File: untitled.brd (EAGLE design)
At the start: 59.4 x 57.8 mm, 25 parts

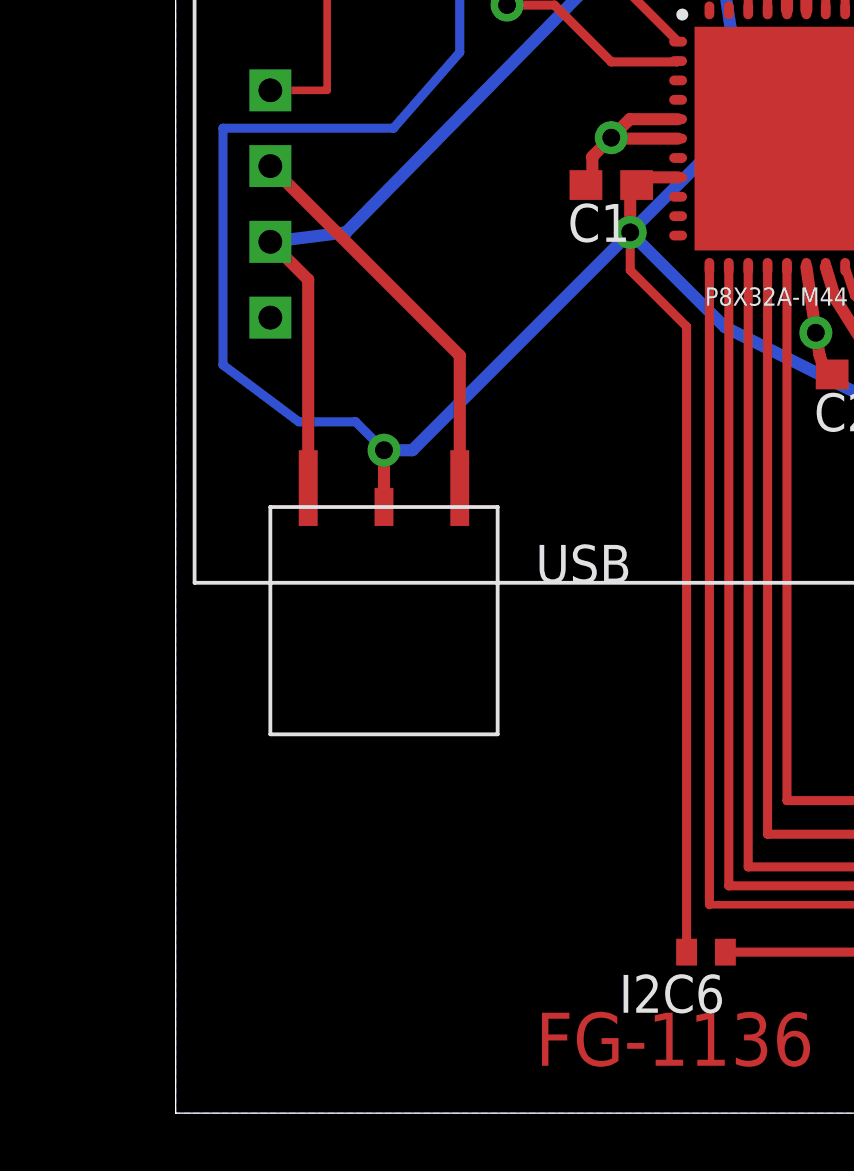
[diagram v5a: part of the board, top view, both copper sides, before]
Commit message: Use regulator part from eagle library
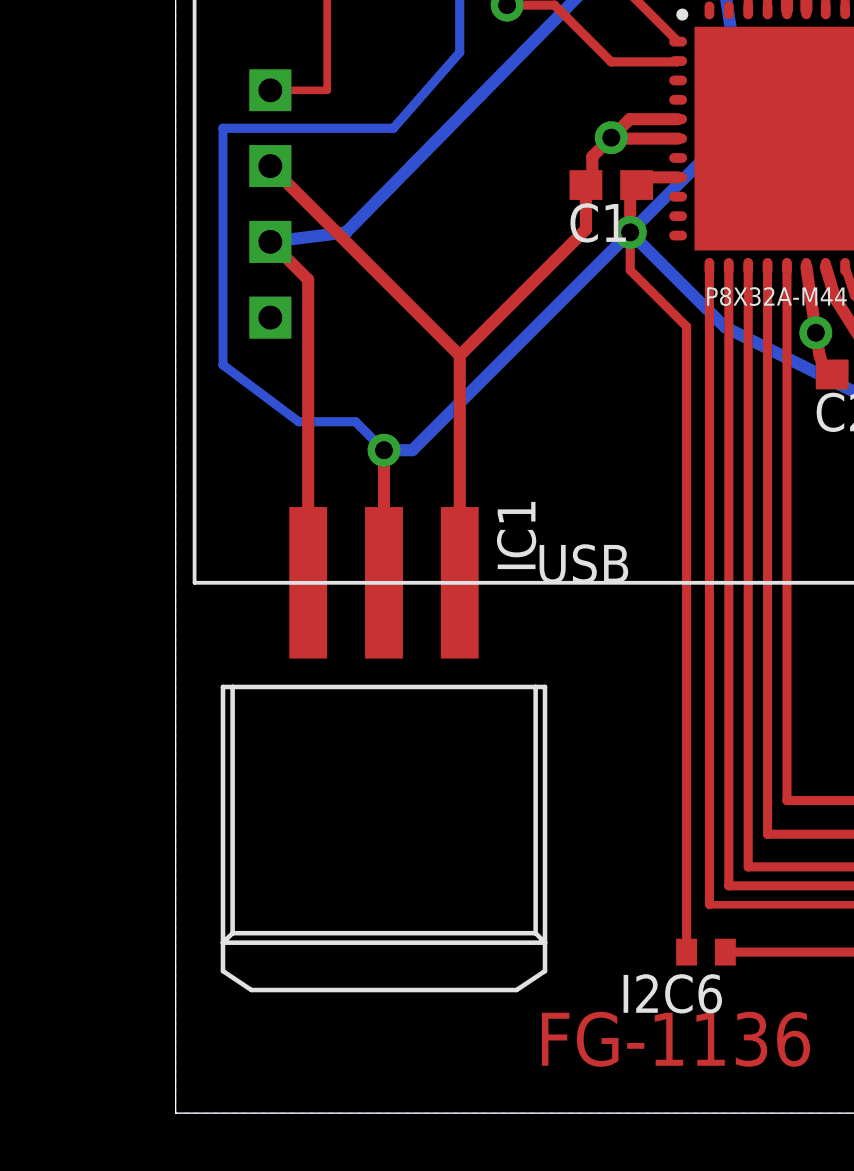
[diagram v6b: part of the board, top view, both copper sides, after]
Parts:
- removed 3.3LDO: LDO1117-33, ldo1117-33:1117-33
- added IC1: REG1117F, burr-brown:DD-3
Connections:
- net +3V3: now also IC1.2; no longer 3.3LDO.VOUT
- net +5V: now also IC1.3; no longer 3.3LDO.VIN
- net GND: now also IC1.1; no longer 3.3LDO.GND
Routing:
- net GND: track 80.1 -> 91.3 mm
- net +5V: track 48.8 -> 52.6 mm
- net +3V3: track 289.7 -> 292.2 mm
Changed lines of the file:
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@@
 </classes>
 <designrules name="SparkFun">
-<description language="C">&lt;b&gt;EAGLE Design Rules&lt;/b&gt;
+<description language="en">&lt;b&gt;EAGLE Design Rules&lt;/b&gt;
 &lt;p&gt;
 The default Design Rules have been set to cover
@@
 </autorouter>
 <elements>
-<element name="3.3LDO" library="ldo1117-33" package="1117-33" value="LDO1117-33" x="40.64" y="26.67" rot="R180"/>
 <element name="5WAYSWITCH" library="5-wayswitch" package="5-WAYSWITCH" value="5-WAYSWITCH" x="64.77" y="16.51"/>
 <element name="EEPROM" library="adafruit" package="DIL08" value="DS1307" x="85.725" y="59.055" rot="R270"/>
@@
 <element name="C3" library="rcl" package="C0603" value="" x="53.6575" y="51.1175" rot="R90"/>
 <element name="C4" library="SparkFun" package="0603" value="" x="79.6925" y="25.0825" rot="R90"/>
+<element name="IC1" library="burr-brown" package="DD-3" value="REG1117F" x="40.64" y="20.0025" rot="R180">
+<attribute name="OC_NEWARK" value="87H2562" x="40.64" y="20.0025" size="1.778" layer="27" rot="R180" display="off"/>
+<attribute name="MPN" value="REG1117FAKTTT" x="40.64" y="20.0025" size="1.778" layer="27" rot="R180" display="off"/>
+<attribute name="MF" value="TEXAS INSTRUMENTS" x="40.64" y="20.0025" size="1.778" layer="27" rot="R180" display="off"/>
+<attribute name="OC_FARNELL" value="1296120" x="40.64" y="20.0025" size="1.778" layer="27" rot="R180" display="off"/>
+</element>
 </elements>
 <signals>
@@
 <contactref element="EEPROM" pad="2"/>
 <contactref element="GPS" pad="P$8"/>
-<contactref element="3.3LDO" pad="GND"/>
 <contactref element="U$2" pad="25"/>
 <contactref element="U$2" pad="29"/>
@@
 <via x="60.6425" y="41.5925" extent="1-16" drill="0.6"/>
 <wire x1="55.245" y1="35.56" x2="55.1175" y2="36.3225" width="0.4064" layer="1"/>
-<wire x1="43.18" y1="31.75" x2="43.18" y2="35.56" width="0.4064" layer="1"/>
 <wire x1="43.18" y1="35.56" x2="36.83" y2="41.91" width="0.4064" layer="1"/>
 <wire x1="89.395" y1="27.895" x2="89.395" y2="25.54" width="0.3048" layer="1"/>
@@
 <wire x1="53.6575" y1="52.07" x2="53.6575" y2="51.9675" width="0.4064" layer="1"/>
 <wire x1="53.6575" y1="52.07" x2="54.8" y2="52.07" width="0.4064" layer="1"/>
+<contactref element="IC1" pad="1"/>
+<wire x1="43.18" y1="27.94" x2="43.18" y2="35.56" width="0.4064" layer="1"/>
+<wire x1="47.41" y1="41.275" x2="47.41" y2="39.79" width="0.4064" layer="1"/>
+<wire x1="47.41" y1="39.79" x2="43.18" y2="35.56" width="0.4064" layer="1"/>
 </signal>
 <signal name="+5V">
-<contactref element="3.3LDO" pad="VIN"/>
 <contactref element="LIPOCHARGER-BOOSTER" pad="VCC"/>
 <contactref element="OLED_SCREEN" pad="5V"/>
-<wire x1="38.1" y1="31.75" x2="38.1" y2="38.1" width="0.4064" layer="1"/>
 <wire x1="38.1" y1="38.1" x2="36.83" y2="39.37" width="0.4064" layer="1"/>
 <wire x1="36.83" y1="39.37" x2="39.37" y2="39.6875" width="0.4064" layer="16"/>
@@
 <wire x1="57.15" y1="57.785" x2="67.945" y2="57.785" width="0.4064" layer="16"/>
 <wire x1="67.945" y1="57.785" x2="67.945" y2="59.69" width="0.4064" layer="16"/>
+<contactref element="IC1" pad="3"/>
+<wire x1="38.1" y1="27.94" x2="38.1" y2="38.1" width="0.4064" layer="1"/>
 </signal>
 <signal name="+3V3">
-<contactref element="3.3LDO" pad="VOUT"/>
 <contactref element="I2C3" pad="2"/>
 <contactref element="I2C4" pad="2"/>
@@
 <wire x1="55.45" y1="38.5313" x2="55.7675" y2="37.475" width="0.4064" layer="1"/>
 <wire x1="54.15" y1="47.1313" x2="54.15" y2="48.1875" width="0.4064" layer="1"/>
-<wire x1="40.64" y1="30.48" x2="40.64" y2="32.385" width="0.4064" layer="1"/>
 <via x="40.64" y="32.385" extent="1-16" drill="0.6"/>
 <wire x1="40.64" y1="32.385" x2="41.5925" y2="32.385" width="0.4064" layer="16"/>
@@
 <wire x1="63.1825" y1="22.225" x2="73.65438125" y2="22.225" width="0.3048" layer="16"/>
 <wire x1="73.65438125" y1="22.225" x2="73.6993375" y2="22.26995625" width="0.3048" layer="16"/>
+<contactref element="IC1" pad="2"/>
+<wire x1="40.64" y1="27.94" x2="40.64" y2="32.385" width="0.4064" layer="1"/>
 </signal>
 </signals>

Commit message: DRC cleanup
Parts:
- moved C2 0.45 mm to (56.2, 34.6)
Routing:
- net +3V3: track 292.2 -> 293.7 mm
- net N$11: track 32.5 -> 33.6 mm
- net N$16: track 0.64 -> 0.00 mm
- net GND: track 91.3 -> 92.0 mm

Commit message: Lots of improvements
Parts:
- IC1: value REG1117F -> REG1117X; device burr-brown:DD-3 -> burr-brown:TO252
- moved I2C2 46.4 mm to (78.7, 30.5)
- moved I2C 41.8 mm to (78.7, 28.6)
- moved IC1 8.90 mm to (41.0, 28.9)
- moved THERMO 1.42 mm to (42.5, 64.8)
- turned C4 to 180 degrees
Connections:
- net +3V3: now also IC1.3; no longer IC1.2
- net +5V: now also IC1.2; no longer IC1.3
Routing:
- net +3V3: track 293.7 -> 252.8 mm, vias 10 -> 8
- net SCL: track 103.3 -> 109.8 mm, vias 2 -> 1
- net +5V: track 52.6 -> 48.0 mm
- net GND: track 92.0 -> 89.6 mm
- net SDA: track 97.0 -> 97.1 mm, vias 2 -> 1
